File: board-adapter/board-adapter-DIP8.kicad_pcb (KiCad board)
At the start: 2 copper layers, 14.8 x 11.2 mm, 3 parts, among them J101 Conn_01x04, J102 Conn_02x04_Odd_Even, J103 Conn_01x04

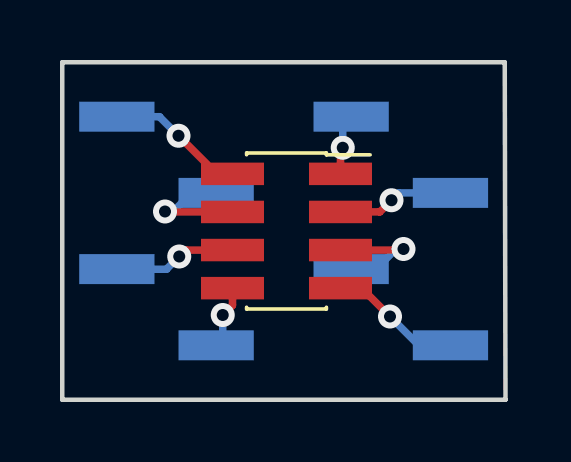
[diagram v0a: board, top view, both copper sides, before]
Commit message: increase trace width
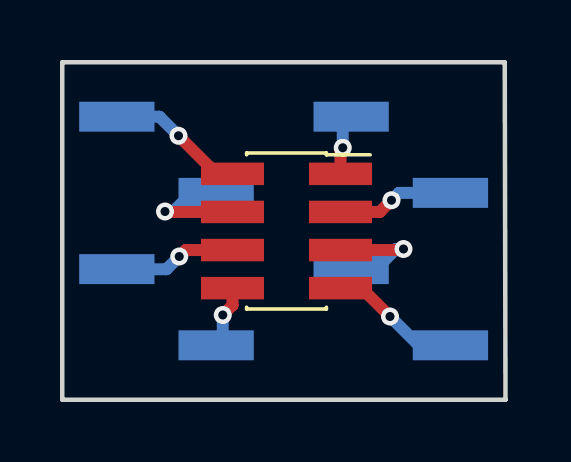
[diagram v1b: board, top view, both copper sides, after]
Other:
- net class Default: trace_width 0.25 -> 0.4; via_dia 0.8 -> 0.6; via_drill 0.4 -> 0.3
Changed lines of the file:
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@@
   )
   (setup
-    (last_trace_width 0.25)
+    (last_trace_width 0.4)
     (trace_clearance 0.2)
     (zone_clearance 0.508)
@@
     (segment_width 0.2)
     (edge_width 0.15)
-    (via_size 0.8)
-    (via_drill 0.4)
+    (via_size 0.6)
+    (via_drill 0.3)
     (via_min_size 0.4)
     (via_min_drill 0.3)
@@
   (net_class Default "This is the default net class."
     (clearance 0.2)
-    (trace_width 0.25)
-    (via_dia 0.8)
-    (via_drill 0.4)
+    (trace_width 0.4)
+    (via_dia 0.6)
+    (via_drill 0.3)
     (uvia_dia 0.3)
     (uvia_drill 0.1)
@@
   (gr_line (start 107.275 94.375) (end 107.3 105.625) (layer Edge.Cuts) (width 0.15))
   (gr_line (start 92.525 94.375) (end 107.275 94.375) (layer Edge.Cuts) (width 0.15))
-  (via (at 95.95 99.35) (size 0.8) (drill 0.4) (layers F.Cu B.Cu) (net 1))
-  (segment (start 95.965 99.365) (end 95.95 99.35) (width 0.25) (layer F.Cu) (net 1))
-  (segment (start 98.2 99.365) (end 95.965 99.365) (width 0.25) (layer F.Cu) (net 1))
-  (segment (start 96.225 99.35) (end 95.95 99.35) (width 0.25) (layer B.Cu) (net 1))
-  (segment (start 96.845 98.73) (end 96.225 99.35) (width 0.25) (layer B.Cu) (net 1))
-  (segment (start 97.655 98.73) (end 96.845 98.73) (width 0.25) (layer B.Cu) (net 1))
-  (via (at 97.875 102.8) (size 0.8) (drill 0.4) (layers F.Cu B.Cu) (net 2))
-  (segment (start 98.2 102.475) (end 97.875 102.8) (width 0.25) (layer F.Cu) (net 2))
-  (segment (start 98.2 101.905) (end 98.2 102.475) (width 0.25) (layer F.Cu) (net 2))
-  (segment (start 97.875 103.59) (end 97.655 103.81) (width 0.25) (layer B.Cu) (net 2))
-  (segment (start 97.875 102.8) (end 97.875 103.59) (width 0.25) (layer B.Cu) (net 2))
-  (segment (start 97.67 98.095) (end 96.4 96.825) (width 0.25) (layer F.Cu) (net 3))
-  (via (at 96.4 96.825) (size 0.8) (drill 0.4) (layers F.Cu B.Cu) (net 3))
-  (segment (start 98.2 98.095) (end 97.67 98.095) (width 0.25) (layer F.Cu) (net 3))
-  (segment (start 95.765 96.19) (end 96.4 96.825) (width 0.25) (layer B.Cu) (net 3))
-  (segment (start 94.345 96.19) (end 95.765 96.19) (width 0.25) (layer B.Cu) (net 3))
-  (via (at 96.425 100.85) (size 0.8) (drill 0.4) (layers F.Cu B.Cu) (net 4))
-  (segment (start 96.64 100.635) (end 96.425 100.85) (width 0.25) (layer F.Cu) (net 4))
-  (segment (start 98.2 100.635) (end 96.64 100.635) (width 0.25) (layer F.Cu) (net 4))
-  (segment (start 94.35 101.275) (end 94.345 101.27) (width 0.25) (layer B.Cu) (net 4))
-  (segment (start 96 101.275) (end 94.35 101.275) (width 0.25) (layer B.Cu) (net 4))
-  (segment (start 96.425 100.85) (end 96 101.275) (width 0.25) (layer B.Cu) (net 4))
-  (via (at 101.875 97.225) (size 0.8) (drill 0.4) (layers F.Cu B.Cu) (net 5))
-  (segment (start 101.8 97.3) (end 101.875 97.225) (width 0.25) (layer F.Cu) (net 5))
-  (segment (start 101.8 98.095) (end 101.8 97.3) (width 0.25) (layer F.Cu) (net 5))
-  (segment (start 101.875 96.47) (end 102.155 96.19) (width 0.25) (layer B.Cu) (net 5))
-  (segment (start 101.875 97.225) (end 101.875 96.47) (width 0.25) (layer B.Cu) (net 5))
-  (via (at 103.5 98.975) (size 0.8) (drill 0.4) (layers F.Cu B.Cu) (net 6))
-  (segment (start 103.11 99.365) (end 103.5 98.975) (width 0.25) (layer F.Cu) (net 6))
-  (segment (start 101.8 99.365) (end 103.11 99.365) (width 0.25) (layer F.Cu) (net 6))
-  (segment (start 103.745 98.73) (end 103.5 98.975) (width 0.25) (layer B.Cu) (net 6))
-  (segment (start 105.465 98.73) (end 103.745 98.73) (width 0.25) (layer B.Cu) (net 6))
-  (segment (start 103.865 100.635) (end 103.9 100.6) (width 0.25) (layer F.Cu) (net 7))
-  (segment (start 101.8 100.635) (end 103.865 100.635) (width 0.25) (layer F.Cu) (net 7))
-  (via (at 103.9 100.6) (size 0.8) (drill 0.4) (layers F.Cu B.Cu) (net 7))
-  (segment (start 103.65 100.6) (end 103.9 100.6) (width 0.25) (layer B.Cu) (net 7))
-  (segment (start 102.98 101.27) (end 103.65 100.6) (width 0.25) (layer B.Cu) (net 7))
-  (segment (start 102.155 101.27) (end 102.98 101.27) (width 0.25) (layer B.Cu) (net 7))
-  (via (at 103.45 102.85) (size 0.8) (drill 0.4) (layers F.Cu B.Cu) (net 8))
-  (segment (start 102.505 101.905) (end 103.45 102.85) (width 0.25) (layer F.Cu) (net 8))
-  (segment (start 101.8 101.905) (end 102.505 101.905) (width 0.25) (layer F.Cu) (net 8))
-  (segment (start 104.41 103.81) (end 103.45 102.85) (width 0.25) (layer B.Cu) (net 8))
-  (segment (start 105.465 103.81) (end 104.41 103.81) (width 0.25) (layer B.Cu) (net 8))
+  (via (at 95.95 99.35) (size 0.6) (drill 0.3) (layers F.Cu B.Cu) (net 1))
+  (segment (start 95.965 99.365) (end 95.95 99.35) (width 0.4) (layer F.Cu) (net 1))
+  (segment (start 98.2 99.365) (end 95.965 99.365) (width 0.4) (layer F.Cu) (net 1))
+  (segment (start 96.225 99.35) (end 95.95 99.35) (width 0.4) (layer B.Cu) (net 1))
+  (segment (start 96.845 98.73) (end 96.225 99.35) (width 0.4) (layer B.Cu) (net 1))
+  (segment (start 97.655 98.73) (end 96.845 98.73) (width 0.4) (layer B.Cu) (net 1))
+  (via (at 97.875 102.8) (size 0.6) (drill 0.3) (layers F.Cu B.Cu) (net 2))
+  (segment (start 98.2 102.475) (end 97.875 102.8) (width 0.4) (layer F.Cu) (net 2))
+  (segment (start 98.2 101.905) (end 98.2 102.475) (width 0.4) (layer F.Cu) (net 2))
+  (segment (start 97.875 103.59) (end 97.655 103.81) (width 0.4) (layer B.Cu) (net 2))
+  (segment (start 97.875 102.8) (end 97.875 103.59) (width 0.4) (layer B.Cu) (net 2))
+  (segment (start 97.67 98.095) (end 96.4 96.825) (width 0.4) (layer F.Cu) (net 3))
+  (via (at 96.4 96.825) (size 0.6) (drill 0.3) (layers F.Cu B.Cu) (net 3))
+  (segment (start 98.2 98.095) (end 97.67 98.095) (width 0.4) (layer F.Cu) (net 3))
+  (segment (start 95.765 96.19) (end 96.4 96.825) (width 0.4) (layer B.Cu) (net 3))
+  (segment (start 94.345 96.19) (end 95.765 96.19) (width 0.4) (layer B.Cu) (net 3))
+  (via (at 96.425 100.85) (size 0.6) (drill 0.3) (layers F.Cu B.Cu) (net 4))
+  (segment (start 96.64 100.635) (end 96.425 100.85) (width 0.4) (layer F.Cu) (net 4))
+  (segment (start 98.2 100.635) (end 96.64 100.635) (width 0.4) (layer F.Cu) (net 4))
+  (segment (start 94.35 101.275) (end 94.345 101.27) (width 0.4) (layer B.Cu) (net 4))
+  (segment (start 96 101.275) (end 94.35 101.275) (width 0.4) (layer B.Cu) (net 4))
+  (segment (start 96.425 100.85) (end 96 101.275) (width 0.4) (layer B.Cu) (net 4))
+  (via (at 101.875 97.225) (size 0.6) (drill 0.3) (layers F.Cu B.Cu) (net 5))
+  (segment (start 101.8 97.3) (end 101.875 97.225) (width 0.4) (layer F.Cu) (net 5))
+  (segment (start 101.8 98.095) (end 101.8 97.3) (width 0.4) (layer F.Cu) (net 5))
+  (segment (start 101.875 96.47) (end 102.155 96.19) (width 0.4) (layer B.Cu) (net 5))
+  (segment (start 101.875 97.225) (end 101.875 96.47) (width 0.4) (layer B.Cu) (net 5))
+  (via (at 103.5 98.975) (size 0.6) (drill 0.3) (layers F.Cu B.Cu) (net 6))
+  (segment (start 103.11 99.365) (end 103.5 98.975) (width 0.4) (layer F.Cu) (net 6))
+  (segment (start 101.8 99.365) (end 103.11 99.365) (width 0.4) (layer F.Cu) (net 6))
+  (segment (start 103.745 98.73) (end 103.5 98.975) (width 0.4) (layer B.Cu) (net 6))
+  (segment (start 105.465 98.73) (end 103.745 98.73) (width 0.4) (layer B.Cu) (net 6))
+  (segment (start 103.865 100.635) (end 103.9 100.6) (width 0.4) (layer F.Cu) (net 7))
+  (segment (start 101.8 100.635) (end 103.865 100.635) (width 0.4) (layer F.Cu) (net 7))
+  (via (at 103.9 100.6) (size 0.6) (drill 0.3) (layers F.Cu B.Cu) (net 7))
+  (segment (start 103.65 100.6) (end 103.9 100.6) (width 0.4) (layer B.Cu) (net 7))
+  (segment (start 102.98 101.27) (end 103.65 100.6) (width 0.4) (layer B.Cu) (net 7))
+  (segment (start 102.155 101.27) (end 102.98 101.27) (width 0.4) (layer B.Cu) (net 7))
+  (via (at 103.45 102.85) (size 0.6) (drill 0.3) (layers F.Cu B.Cu) (net 8))
+  (segment (start 102.505 101.905) (end 103.45 102.85) (width 0.4) (layer F.Cu) (net 8))
+  (segment (start 101.8 101.905) (end 102.505 101.905) (width 0.4) (layer F.Cu) (net 8))
+  (segment (start 104.41 103.81) (end 103.45 102.85) (width 0.4) (layer B.Cu) (net 8))
+  (segment (start 105.465 103.81) (end 104.41 103.81) (width 0.4) (layer B.Cu) (net 8))
 )

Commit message: remove pin 1 markers from wrong position
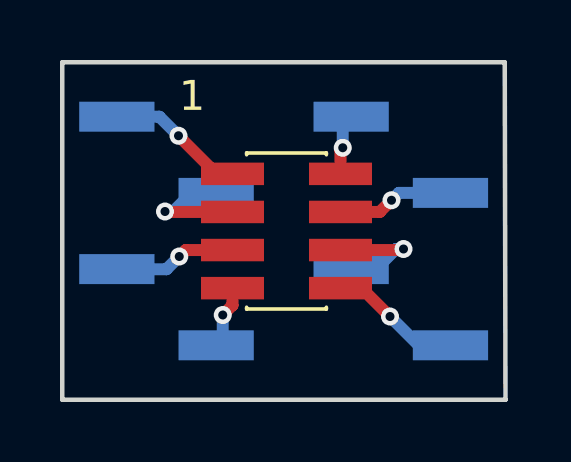
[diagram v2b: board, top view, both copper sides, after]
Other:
- board text added: "1"

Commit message: board-adapter-DIP8: fix slightly wrong pitch
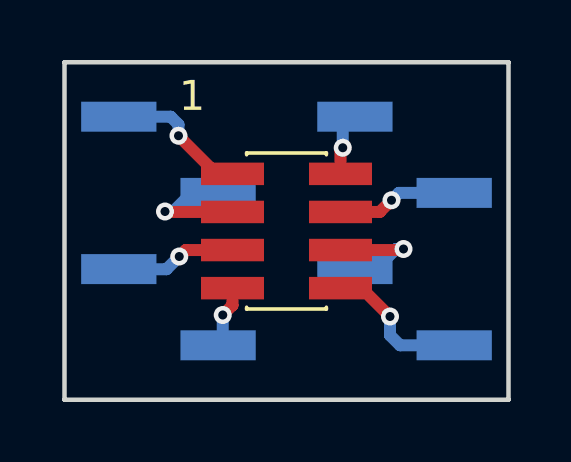
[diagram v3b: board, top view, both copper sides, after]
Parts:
- moved J103 0.12 mm to (103.9, 100.0)
- moved J101 0.06 mm to (96.1, 100.0)
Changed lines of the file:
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@@
     (thickness 1.6)
     (drawings 5)
-    (tracks 43)
+    (tracks 45)
     (zones 0)
     (modules 3)
@@
   )
   (module Connector_PinHeader_2.54mm:PinHeader_1x04_P2.54mm_Vertical_SMD_Pin1Right (layer B.Cu)
-    (at 103.81 100)
+    (at 103.935 100)
     (descr "surface-mounted straight pin header, 1x04, 2.54mm pitch, single row, style 2 (pin 1 right)")
     (tags "Surface mounted pin header SMD 1x04 2.54mm single row style2 pin1 right")
@@
   )
   (module Connector_PinHeader_2.54mm:PinHeader_1x04_P2.54mm_Vertical_SMD_Pin1Right (layer B.Cu)
-    (at 96 100 180)
+    (at 96.065 100 180)
     (descr "surface-mounted straight pin header, 1x04, 2.54mm pitch, single row, style 2 (pin 1 right)")
     (tags "Surface mounted pin header SMD 1x04 2.54mm single row style2 pin1 right")
@@
     (effects (font (size 1 1) (thickness 0.25)))
   )
-  (gr_line (start 92.525 105.625) (end 92.525 94.375) (layer Edge.Cuts) (width 0.15))
-  (gr_line (start 107.3 105.625) (end 92.525 105.625) (layer Edge.Cuts) (width 0.15))
-  (gr_line (start 107.275 94.375) (end 107.3 105.625) (layer Edge.Cuts) (width 0.15))
-  (gr_line (start 92.525 94.375) (end 107.275 94.375) (layer Edge.Cuts) (width 0.15))
+  (gr_line (start 92.6 105.625) (end 92.6 94.375) (layer Edge.Cuts) (width 0.15))
+  (gr_line (start 107.4 105.625) (end 92.6 105.625) (layer Edge.Cuts) (width 0.15))
+  (gr_line (start 107.4 94.375) (end 107.4 105.625) (layer Edge.Cuts) (width 0.15))
+  (gr_line (start 92.6 94.375) (end 107.4 94.375) (layer Edge.Cuts) (width 0.15))
   (via (at 95.95 99.35) (size 0.6) (drill 0.3) (layers F.Cu B.Cu) (net 1))
   (segment (start 95.965 99.365) (end 95.95 99.35) (width 0.4) (layer F.Cu) (net 1))
@@
   (via (at 96.4 96.825) (size 0.6) (drill 0.3) (layers F.Cu B.Cu) (net 3))
   (segment (start 98.2 98.095) (end 97.67 98.095) (width 0.4) (layer F.Cu) (net 3))
-  (segment (start 95.765 96.19) (end 96.4 96.825) (width 0.4) (layer B.Cu) (net 3))
-  (segment (start 94.345 96.19) (end 95.765 96.19) (width 0.4) (layer B.Cu) (net 3))
+  (segment (start 96.14 96.19) (end 96.4 96.45) (width 0.4) (layer B.Cu) (net 3))
+  (segment (start 96.4 96.45) (end 96.4 96.825) (width 0.4) (layer B.Cu) (net 3))
+  (segment (start 94.345 96.19) (end 96.14 96.19) (width 0.4) (layer B.Cu) (net 3))
   (via (at 96.425 100.85) (size 0.6) (drill 0.3) (layers F.Cu B.Cu) (net 4))
   (segment (start 96.64 100.635) (end 96.425 100.85) (width 0.4) (layer F.Cu) (net 4))
@@
   (segment (start 102.505 101.905) (end 103.45 102.85) (width 0.4) (layer F.Cu) (net 8))
   (segment (start 101.8 101.905) (end 102.505 101.905) (width 0.4) (layer F.Cu) (net 8))
-  (segment (start 104.41 103.81) (end 103.45 102.85) (width 0.4) (layer B.Cu) (net 8))
-  (segment (start 105.465 103.81) (end 104.41 103.81) (width 0.4) (layer B.Cu) (net 8))
+  (segment (start 103.785 103.81) (end 103.45 103.475) (width 0.4) (layer B.Cu) (net 8))
+  (segment (start 103.45 103.475) (end 103.45 102.85) (width 0.4) (layer B.Cu) (net 8))
+  (segment (start 105.465 103.81) (end 103.785 103.81) (width 0.4) (layer B.Cu) (net 8))
 )

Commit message: update pad to mask clearance
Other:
- rule pad_to_mask_clearance: 0.2 -> 0.1
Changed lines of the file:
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@@
     (pad_size 1.524 1.524)
     (pad_drill 0.762)
-    (pad_to_mask_clearance 0.2)
+    (pad_to_mask_clearance 0.1)
     (aux_axis_origin 0 0)
     (visible_elements FFFFFF7F)
